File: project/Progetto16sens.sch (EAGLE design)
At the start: 124 parts, among them IC1 LMZ14202TZE-ADJ_NOPB, M1 43650-0201, M2 43650-0201, M3 43650-0201, M4 43650-0201

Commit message: felt like it todaygit add . the aesthetic is coming in, but i dont know how to do things help
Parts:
- removed SV3, SV4: (no value), con-lstb:MA12-1
- added L_BALL: (no value), led:LEDCHIPLED_1206
- added R_BALL: (no value), rcl:R-EU_M0805
- added SW_BALL: TL38PO, switch:TL38PO
- SV1, SV2, SV5: device con-lstb:MA12-1 -> con-lsta:FE12-1
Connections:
- new net N$60: BALL_MUX.!E, SW_BALL.P
- new net N$61: R_BALL.2, SW_BALL.O
- new net N$62: L_BALL.A, R_BALL.1
- new net PWB_1: BALL_MUX.S0
- new net PWB_2: BALL_MUX.S1
- new net PWB_3: BALL_MUX.S2
- new net PWB_4: BALL_MUX.S3
- net +3V3: now also BALL_MUX.VCC, SW_BALL.S
- net B1: now also BALL_MUX.I0; no longer SV2.3, U$1.10-CS/MQSR
- net B10: now also BALL_MUX.I9
- net B11: now also BALL_MUX.I10
- net B12: now also BALL_MUX.I11
- net B13: now also BALL_MUX.I12
- net B14: now also BALL_MUX.I13
- net B15: now also BALL_MUX.I14
- net B16: now also BALL_MUX.I15
- net B2: now also BALL_MUX.I1; no longer SV2.4, U$1.11-MOSI/CTX1
- net B3: now also BALL_MUX.I2
- net B4: now also BALL_MUX.I3
- net B5: now also BALL_MUX.I4
- net B6: now also BALL_MUX.I5
- net B7: now also BALL_MUX.I6
- net B8: now also BALL_MUX.I7
- net B9: now also BALL_MUX.I8
- net GND: now also L_BALL.C
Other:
- moved on the sheet: BALL_MUX, SV6

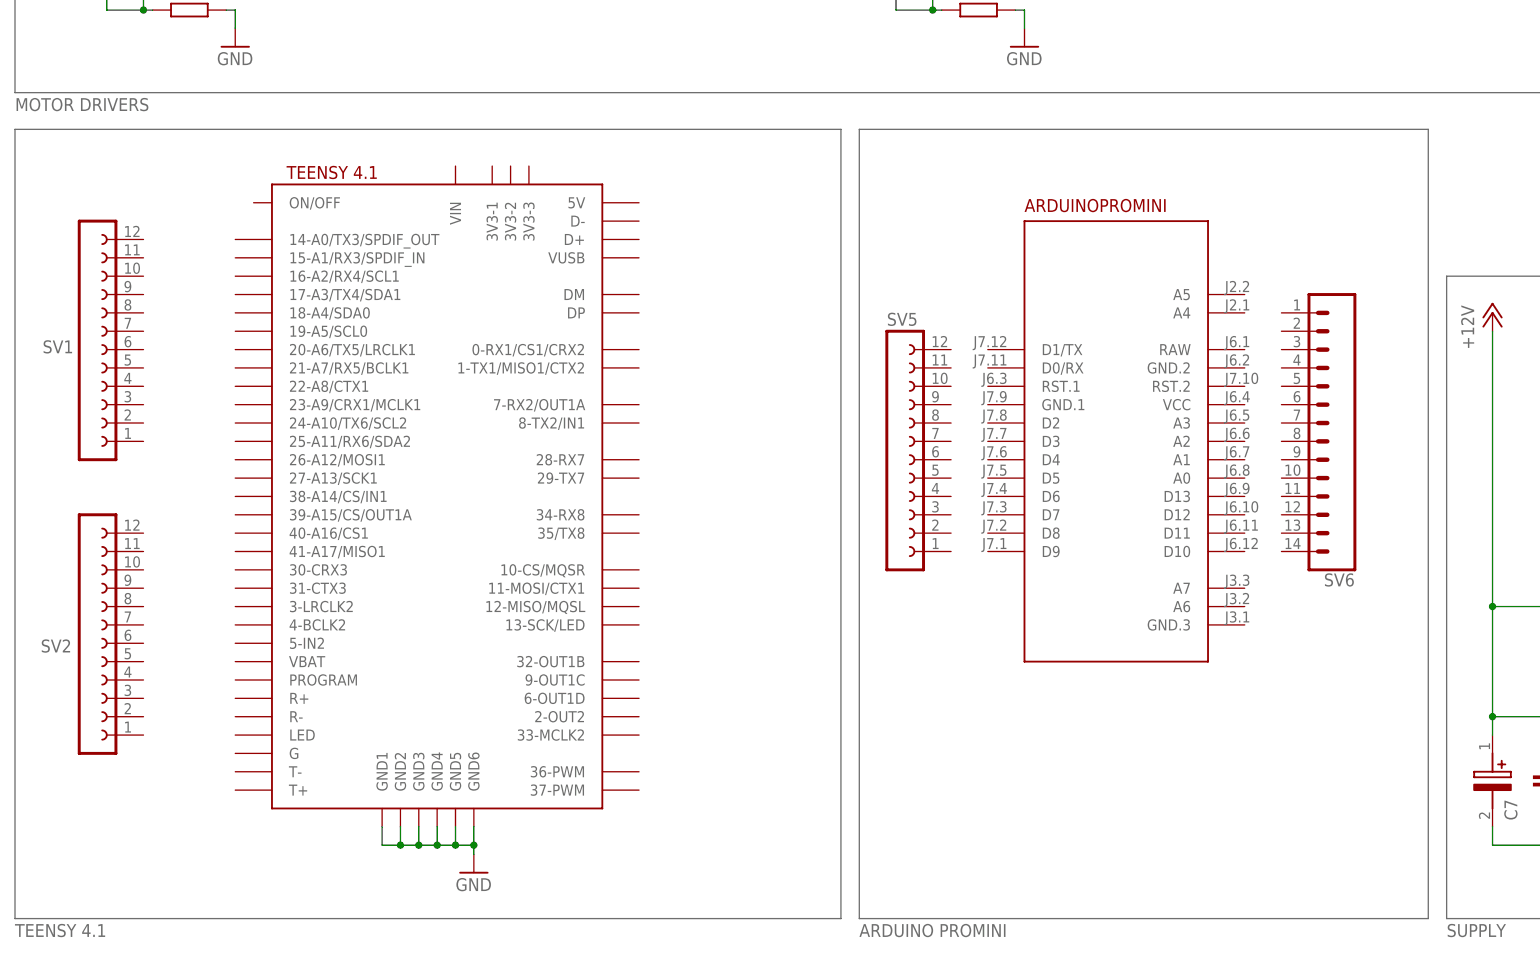
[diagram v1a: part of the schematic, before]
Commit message: added cons, starting wiring (hopefully)
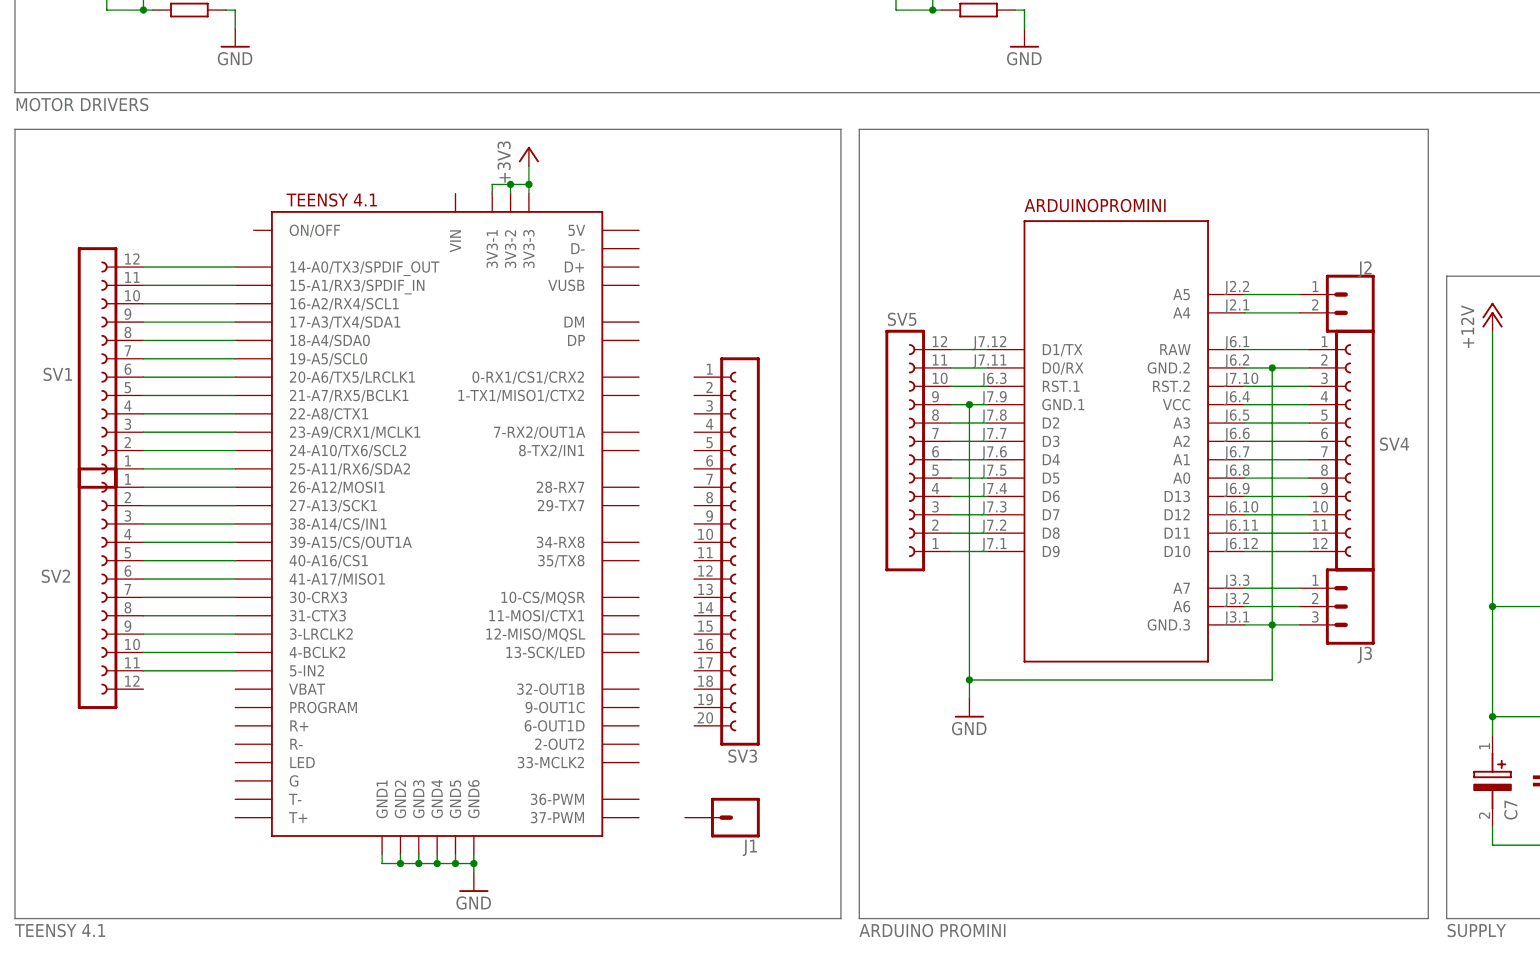
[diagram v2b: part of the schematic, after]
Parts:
- removed SV6: (no value), SparkFun-Connectors:CONN_14LONGPADS
- added J1: (no value), SparkFun-Connectors:CONN_01
- added J2: (no value), SparkFun-Connectors:CONN_02
- added J3: 455-1750-1-ND, SparkFun-Connectors:CONN_03
- added SV3: (no value), con-lsta:FE20-1
- added SV4: (no value), con-lsta:FE12-1
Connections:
- new net N$37: SV1.11, U$1.15-A1/RX3/SPDIF_IN
- new net N$38: SV1.10, U$1.16-A2/RX4/SCL1
- new net N$40: SV1.9, U$1.17-A3/TX4/SDA1
- new net N$41: SV1.8, U$1.18-A4/SDA0
- new net N$42: SV1.7, U$1.19-A5/SCL0
- new net N$43: SV1.6, U$1.20-A6/TX5/LRCLK1
- new net N$44: SV1.5, U$1.21-A7/RX5/BCLK1
- new net N$45: SV1.4, U$1.22-A8/CTX1
- new net N$46: SV1.3, U$1.23-A9/CRX1/MCLK1
- new net N$47: SV1.2, U$1.24-A10/TX6/SCL2
- new net N$48: SV1.1, U$1.25-A11/RX6/SDA2
- new net N$49: SV2.1, U$1.26-A12/MOSI1
- new net N$5: SV1.12, U$1.14-A0/TX3/SPDIF_OUT
- new net N$50: SV2.2, U$1.27-A13/SCK1
- new net N$51: SV2.3, U$1.38-A14/CS/IN1
- new net N$52: SV2.4, U$1.39-A15/CS/OUT1A
- new net N$53: SV2.5, U$1.40-A16/CS1
- new net N$54: SV2.6, U$1.41-A17/MISO1
- new net N$55: SV2.7, U$1.30-CRX3
- new net N$56: SV2.8, U$1.31-CTX3
- new net N$57: SV2.9, U$1.3-LRCLK2
- new net N$58: SV2.10, U$1.4-BCLK2
- new net N$59: SV2.11, U$1.5-IN2
- new net N$63: ARDUINOPROMINI.D1/TX, SV5.12
- new net N$64: ARDUINOPROMINI.D0/RX, SV5.11
- new net N$65: ARDUINOPROMINI.RST.1, SV5.10
- new net N$67: ARDUINOPROMINI.D2, SV5.8
- new net N$68: ARDUINOPROMINI.D3, SV5.7
- new net N$69: ARDUINOPROMINI.D4, SV5.6
- new net N$70: ARDUINOPROMINI.D5, SV5.5
- new net N$71: ARDUINOPROMINI.D6, SV5.4
- new net N$72: ARDUINOPROMINI.D7, SV5.3
- new net N$73: ARDUINOPROMINI.D8, SV5.2
- new net N$74: ARDUINOPROMINI.D9, SV5.1
- new net N$75: ARDUINOPROMINI.A5, J2.1
- new net N$76: ARDUINOPROMINI.A4, J2.2
- new net N$77: ARDUINOPROMINI.A7, J3.1
- new net N$78: ARDUINOPROMINI.A6, J3.2
- new net N$80: ARDUINOPROMINI.RAW, SV4.1
- new net N$82: ARDUINOPROMINI.RST.2, SV4.3
- new net N$83: ARDUINOPROMINI.VCC, SV4.4
- new net N$84: ARDUINOPROMINI.A3, SV4.5
- new net N$85: ARDUINOPROMINI.A2, SV4.6
- new net N$86: ARDUINOPROMINI.A1, SV4.7
- new net N$87: ARDUINOPROMINI.A0, SV4.8
- new net N$88: ARDUINOPROMINI.D13, SV4.9
- new net N$89: ARDUINOPROMINI.D12, SV4.10
- new net N$90: ARDUINOPROMINI.D11, SV4.11
- new net N$91: ARDUINOPROMINI.D10, SV4.12
- net +3V3: now also U$1.3V3-1, U$1.3V3-2, U$1.3V3-3
- net GND: now also ARDUINOPROMINI.GND.1, ARDUINOPROMINI.GND.2, ARDUINOPROMINI.GND.3, J3.3, SV4.2, SV5.9
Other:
- moved on the sheet: SV1, SV2

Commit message: edited libraries, to edit even further
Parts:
- removed ARDUINOPROMINI: ARDUINO-PRO-MINI-5.0V#NP, arduinopromininew:ARDUINO-PRO-MINI-5.0V#NP
- removed J2: (no value), SparkFun-Connectors:CONN_02
- removed J3: 455-1750-1-ND, SparkFun-Connectors:CONN_03
- removed SV5: (no value), con-lsta:FE12-1
- added M5: ARDUINO-PRO-MINI, arduinopromininew:ARDUINO-PRO-MINI-3.3V#NP
- added SV6: (no value), con-lsta:FE12-1
- J1: device SparkFun-Connectors:CONN_01 -> SparkFun-Connectors:CONN_17
- SV3: device con-lsta:FE20-1 -> con-lsta:FE12-1
- U$1: value TEENSY41 -> TEENSY41_EDIT; device teensy:TEENSY41 -> teensy:TEENSY41_EDIT
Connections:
- new net N$100: SV6.2, U$1.16/A2/RX4/SCL1
- new net N$101: SV6.1, U$1.15/A1/TX3
- new net N$102: SV3.12, U$1.14/A0/TX3
- new net N$103: SV3.11, U$1.13(LED)/SCK
- new net N$104: M5.GND.1, SV4.9
- new net N$105: SV3.9, U$1.41/A17
- new net N$106: SV3.8, U$1.40/A16
- new net N$107: SV3.6, U$1.38/A14/(CS1)
- new net N$108: SV3.7, U$1.39/A15/(MISO1)
- new net N$109: SV3.5, U$1.37/CS
- new net N$110: SV3.4, U$1.36/CS
- new net N$111: SV3.3, U$1.35/TX8
- new net N$112: SV3.2, U$1.34/RX8
- new net N$113: SV3.1, U$1.33
- new net N$114: M5.D7, SV4.3
- new net N$115: M5.D8, SV4.2
- new net N$116: M5.D9, SV4.1
- new net N$66: SV2.1, U$1.32
- new net N$79: SV6.12, U$1.VIN
- new net N$81: J1.6, M5.VCC
- new net N$92: J1.17
- new net N$93: SV6.9, U$1.23/A9
- new net N$94: SV6.8, U$1.22/A8
- new net N$95: SV6.7, U$1.21/A7/RX5
- new net N$96: SV6.6, U$1.20/A6/TX5
- new net N$97: SV6.5, U$1.19/A5/SCL
- new net N$98: SV6.4, U$1.18/A4/SDA
- new net N$99: SV6.3, U$1.17/A3/TX4/SDA1
- net +3V3: no longer U$1.3V3-1, U$1.3V3-2, U$1.3V3-3
- net GND: now also M5.GND.3; no longer ARDUINOPROMINI.GND.1, ARDUINOPROMINI.GND.2, ARDUINOPROMINI.GND.3, J3.3, SV4.2, SV5.9, U$1.GND1, U$1.GND2, U$1.GND3, U$1.GND4, U$1.GND5, U$1.GND6
- net N$37: now also U$1.0/RX1; no longer U$1.15-A1/RX3/SPDIF_IN
- net N$38: now also U$1.1/TX1; no longer U$1.16-A2/RX4/SCL1
- net N$40: now also U$1.2; no longer U$1.17-A3/TX4/SDA1
- net N$41: now also U$1.3; no longer U$1.18-A4/SDA0
- net N$42: now also U$1.4; no longer U$1.19-A5/SCL0
- net N$43: now also U$1.5; no longer U$1.20-A6/TX5/LRCLK1
- net N$44: now also U$1.6; no longer U$1.21-A7/RX5/BCLK1
- net N$45: now also U$1.7/RX2; no longer U$1.22-A8/CTX1
- net N$46: now also U$1.8/TX2; no longer U$1.23-A9/CRX1/MCLK1
- net N$47: now also U$1.9; no longer U$1.24-A10/TX6/SCL2
- net N$48: now also U$1.10/CS; no longer U$1.25-A11/RX6/SDA2
- net N$49: now also SV2.12, U$1.11/MOSI; no longer SV2.1, U$1.26-A12/MOSI1
- net N$5: now also SV2.10, U$1.3V3; no longer SV1.12, U$1.14-A0/TX3/SPDIF_OUT
- net N$50: now also SV2.11, U$1.12/MISO; no longer SV2.2, U$1.27-A13/SCK1
- net N$51: now also SV6.10, U$1.3V3_1; no longer SV2.3, U$1.38-A14/CS/IN1
- net N$52: now also SV2.9, U$1.24/A10/TX6/SCL2; no longer SV2.4, U$1.39-A15/CS/OUT1A
- net N$53: now also SV2.8, U$1.25/A11/RX6/SDA2; no longer SV2.5, U$1.40-A16/CS1
- net N$54: now also SV2.7, U$1.26/A12/MOSI1; no longer SV2.6, U$1.41-A17/MISO1
- net N$55: now also SV2.6, U$1.27/A13/SCK1; no longer SV2.7, U$1.30-CRX3
- net N$56: now also SV2.5, U$1.28/RX7; no longer SV2.8, U$1.31-CTX3
- net N$57: now also SV2.4, U$1.29/TX7; no longer SV2.9, U$1.3-LRCLK2
- net N$58: now also SV2.3, U$1.30; no longer SV2.10, U$1.4-BCLK2
- net N$59: now also SV2.2, U$1.31; no longer SV2.11, U$1.5-IN2
- net N$63: now also J1.1, M5.A5; no longer ARDUINOPROMINI.D1/TX, SV5.12
- net N$64: now also J1.2, M5.A4; no longer ARDUINOPROMINI.D0/RX, SV5.11
- net N$65: now also J1.3, M5.RAW; no longer ARDUINOPROMINI.RST.1, SV5.10
- net N$67: now also SV6.11, U$1.GND_2; no longer ARDUINOPROMINI.D2, SV5.8
- net N$68: now also J1.5, M5.RST.2; no longer ARDUINOPROMINI.D3, SV5.7
- net N$69: now also SV3.10, U$1.GND_1; no longer ARDUINOPROMINI.D4, SV5.6
- net N$70: now also J1.7, M5.A3; no longer ARDUINOPROMINI.D5, SV5.5
- net N$71: now also J1.8, M5.A2; no longer ARDUINOPROMINI.D6, SV5.4
- net N$72: now also J1.9, M5.A1; no longer ARDUINOPROMINI.D7, SV5.3
- net N$73: now also J1.10, M5.A0; no longer ARDUINOPROMINI.D8, SV5.2
- net N$74: now also J1.11, M5.D13; no longer ARDUINOPROMINI.D9, SV5.1
- net N$75: now also J1.12, M5.D12; no longer ARDUINOPROMINI.A5, J2.1
- net N$76: now also J1.13, M5.D11; no longer ARDUINOPROMINI.A4, J2.2
- net N$77: now also J1.14, M5.D10; no longer ARDUINOPROMINI.A7, J3.1
- net N$78: now also J1.15, M5.A7; no longer ARDUINOPROMINI.A6, J3.2
- net N$80: now also J1.16, M5.A6; no longer ARDUINOPROMINI.RAW, SV4.1
- net N$82: now also SV1.12, U$1.GND; no longer ARDUINOPROMINI.RST.2, SV4.3
- net N$83: now also M5.D1/TX, SV4.12; no longer ARDUINOPROMINI.VCC, SV4.4
- net N$84: now also M5.D0/RX, SV4.11; no longer ARDUINOPROMINI.A3, SV4.5
- net N$85: now also M5.RST.1, SV4.10; no longer ARDUINOPROMINI.A2, SV4.6
- net N$86: now also J1.4, M5.GND.2; no longer ARDUINOPROMINI.A1, SV4.7
- net N$87: now also M5.D2; no longer ARDUINOPROMINI.A0
- net N$88: now also M5.D3, SV4.7; no longer ARDUINOPROMINI.D13, SV4.9
- net N$89: now also M5.D4, SV4.6; no longer ARDUINOPROMINI.D12, SV4.10
- net N$90: now also M5.D5, SV4.5; no longer ARDUINOPROMINI.D11, SV4.11
- net N$91: now also M5.D6, SV4.4; no longer ARDUINOPROMINI.D10, SV4.12
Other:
- note added: "TEENSY4.1"
- moved on the sheet: SV1, SV2, SV4
